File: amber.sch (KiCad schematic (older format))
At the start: 46 parts, among them J1 SJ-43504-SMT-TR

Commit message: Replace 2 LEDs with one 5mm
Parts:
- removed D18, D19: LED, LED_THT:LED_D3.0mm, symbol Device:LED
- removed R2: R, Resistor_SMD:R_1206_3216Metric_Pad1.30x1.75mm_HandSolder, symbol Device:R
- added D15: LED_BRCG, LED_THT:LED_D5.0mm-4_RGB_Wide_Pins, symbol Device:LED_BRCG
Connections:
- net LED1: now also D15.1 (BA)
- net LED2: now also D15.4 (GA)
- net LED3: now reaches C1.5 (SDA/D1/2)
- net LED3: now also D15.2 (RA)
- net at R1.2: now also D15.3 (K)
- no-connect marks 4 -> 3
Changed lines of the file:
@@
 Serial
-$Comp
-L Device:LED D18
-U 1 1 6023A331
-P 8250 5425
-F 0 "D18" H 8243 5170 50  0000 C CNN
-F 1 "LED" H 8243 5261 50  0000 C CNN
-F 2 "LED_THT:LED_D3.0mm" H 8250 5425 50  0001 C CNN
-F 3 "~" H 8250 5425 50  0001 C CNN
-	1    8250 5425
-	-1   0    0    1
-$EndComp
 $Comp
 L Device:R R1
@@
 Wire Wire Line
 	8400 5425 8650 5425
-Wire Wire Line
-	8100 5425 7875 5425
-Text GLabel 7875 5425 0    50   Input ~ 0
+Text GLabel 7775 5225 0    50   Input ~ 0
 LED1
 Text GLabel 9750 2900 2    50   Input ~ 0
@@
 Text GLabel 9750 2800 2    50   Input ~ 0
 LED2
-$Comp
-L Device:LED D19
-U 1 1 60247971
-P 8250 6000
-F 0 "D19" H 8243 5745 50  0000 C CNN
-F 1 "LED" H 8243 5836 50  0000 C CNN
-F 2 "LED_THT:LED_D3.0mm" H 8250 6000 50  0001 C CNN
-F 3 "~" H 8250 6000 50  0001 C CNN
-	1    8250 6000
-	-1   0    0    1
-$EndComp
-$Comp
-L Device:R R2
-U 1 1 6024797B
-P 8800 6000
-F 0 "R2" V 8593 6000 50  0000 C CNN
-F 1 "R" V 8684 6000 50  0000 C CNN
-F 2 "Resistor_SMD:R_1206_3216Metric_Pad1.30x1.75mm_HandSolder" V 8730 6000 50  0001 C CNN
-F 3 "~" H 8800 6000 50  0001 C CNN
-	1    8800 6000
-	0    1    1    0
-$EndComp
-$Comp
-L power:GND #PWR08
-U 1 1 60247985
-P 9175 6050
-F 0 "#PWR08" H 9175 5800 50  0001 C CNN
-F 1 "GND" H 9180 5877 50  0000 C CNN
-F 2 "" H 9175 6050 50  0001 C CNN
-F 3 "" H 9175 6050 50  0001 C CNN
-	1    9175 6050
-	1    0    0    -1
-$EndComp
-Wire Wire Line
-	8950 6000 9175 6000
-Wire Wire Line
-	9175 6000 9175 6050
-Wire Wire Line
-	8400 6000 8650 6000
-Wire Wire Line
-	8100 6000 7875 6000
-Text GLabel 7875 6000 0    50   Input ~ 0
+Text GLabel 7775 5425 0    50   Input ~ 0
 LED2
 Wire Wire Line
@@
 Wire Wire Line
 	6450 4025 6450 3925
-NoConn ~ 9750 2200
 NoConn ~ 9025 4650
 $Comp
@@
 Wire Wire Line
 	8350 1675 8350 1800
+$Comp
+L Device:LED_BRCG D15
+U 1 1 604EF23C
+P 8200 5425
+F 0 "D15" H 8200 4958 50  0000 C CNN
+F 1 "LED_BRCG" H 8200 5049 50  0000 C CNN
+F 2 "LED_THT:LED_D5.0mm-4_RGB_Wide_Pins" H 8200 5375 50  0001 C CNN
+F 3 "~" H 8200 5375 50  0001 C CNN
+	1    8200 5425
+	-1   0    0    1
+$EndComp
+Text GLabel 7775 5625 0    50   Input ~ 0
+LED3
+Text GLabel 9750 2200 2    50   Input ~ 0
+LED3
+Wire Wire Line
+	8000 5425 7775 5425
+Wire Wire Line
+	7775 5225 8000 5225
+Wire Wire Line
+	7775 5625 8000 5625
 $EndSCHEMATC

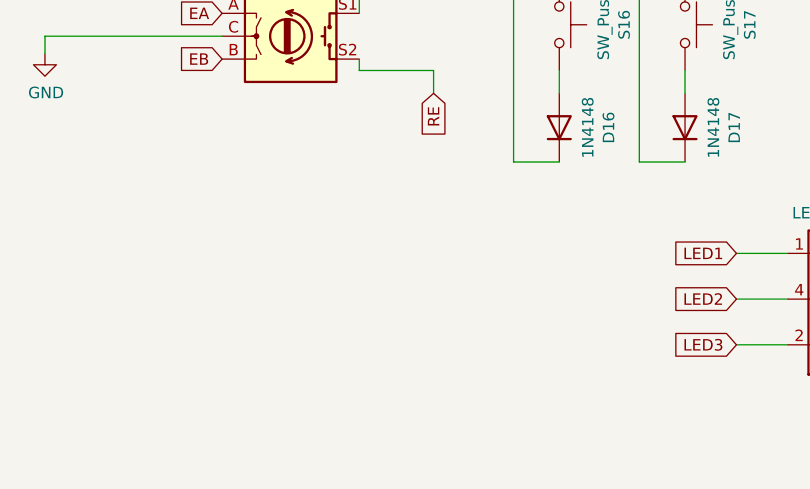
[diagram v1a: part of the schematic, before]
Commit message: Add a pixel LED indicator option
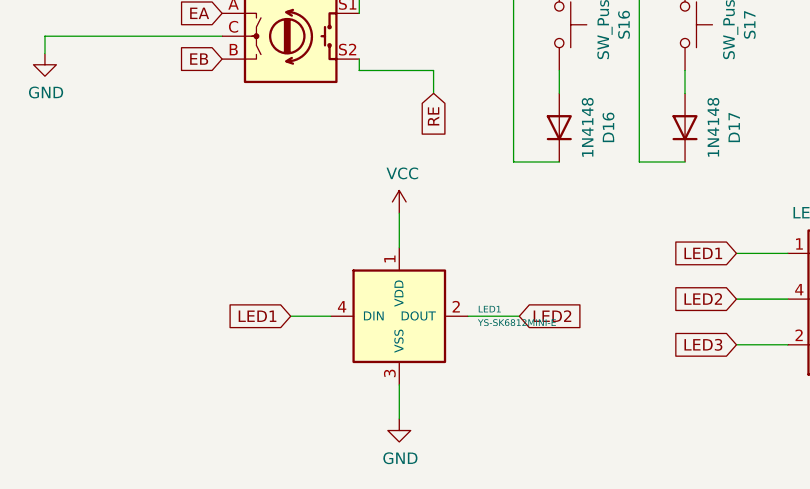
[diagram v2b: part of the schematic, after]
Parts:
- added LED1: YS-SK6812MINI-E, amber:LED_WS2812B-PLCC4-dual, symbol kbd:YS-SK6812MINI-E
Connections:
- net GND: now also LED1.3 (VSS)
- net LED1: now also LED1.4 (DIN)
- net LED2: now also LED1.2 (DOUT)
- net VCC: now also LED1.1 (VDD)
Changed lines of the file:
@@
 Wire Wire Line
 	7775 5625 8000 5625
+$Comp
+L kbd:YS-SK6812MINI-E LED1
+U 1 1 60593469
+P 6300 5500
+F 0 "LED1" H 6644 5530 29  0000 L CNN
+F 1 "YS-SK6812MINI-E" H 6644 5471 29  0000 L CNN
+F 2 "amber:LED_WS2812B-PLCC4-dual" H 6400 5250 50  0001 C CNN
+F 3 "" H 6400 5250 50  0001 C CNN
+	1    6300 5500
+	1    0    0    -1
+$EndComp
+$Comp
+L power:GND #PWR0102
+U 1 1 6059399A
+P 6300 5950
+F 0 "#PWR0102" H 6300 5700 50  0001 C CNN
+F 1 "GND" H 6305 5777 50  0000 C CNN
+F 2 "" H 6300 5950 50  0001 C CNN
+F 3 "" H 6300 5950 50  0001 C CNN
+	1    6300 5950
+	1    0    0    -1
+$EndComp
+$Comp
+L power:VCC #PWR0103
+U 1 1 60593DF0
+P 6300 5050
+F 0 "#PWR0103" H 6300 4900 50  0001 C CNN
+F 1 "VCC" H 6315 5223 50  0000 C CNN
+F 2 "" H 6300 5050 50  0001 C CNN
+F 3 "" H 6300 5050 50  0001 C CNN
+	1    6300 5050
+	1    0    0    -1
+$EndComp
+Wire Wire Line
+	6300 5950 6300 5800
+Wire Wire Line
+	6300 5200 6300 5050
+Text GLabel 5825 5500 0    50   Input ~ 0
+LED1
+Wire Wire Line
+	6000 5500 5825 5500
+Text GLabel 6825 5500 2    50   Input ~ 0
+LED2
+Wire Wire Line
+	6825 5500 6600 5500
 $EndSCHEMATC

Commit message: Make pixel LEDs easier to solder
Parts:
- D15: footprint LED_THT:LED_D5.0mm-4_RGB_Wide_Pins -> amber:LED_D5.0mm-4_RGB_Wide_Pins-dual
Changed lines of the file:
@@
 F 0 "D15" H 8200 4958 50  0000 C CNN
 F 1 "LED_BRCG" H 8200 5049 50  0000 C CNN
-F 2 "LED_THT:LED_D5.0mm-4_RGB_Wide_Pins" H 8200 5375 50  0001 C CNN
+F 2 "amber:LED_D5.0mm-4_RGB_Wide_Pins-dual" H 8200 5375 50  0001 C CNN
 F 3 "~" H 8200 5375 50  0001 C CNN
 	1    8200 5425
